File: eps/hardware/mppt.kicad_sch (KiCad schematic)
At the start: 16 parts, among them U43 LTC3130-1

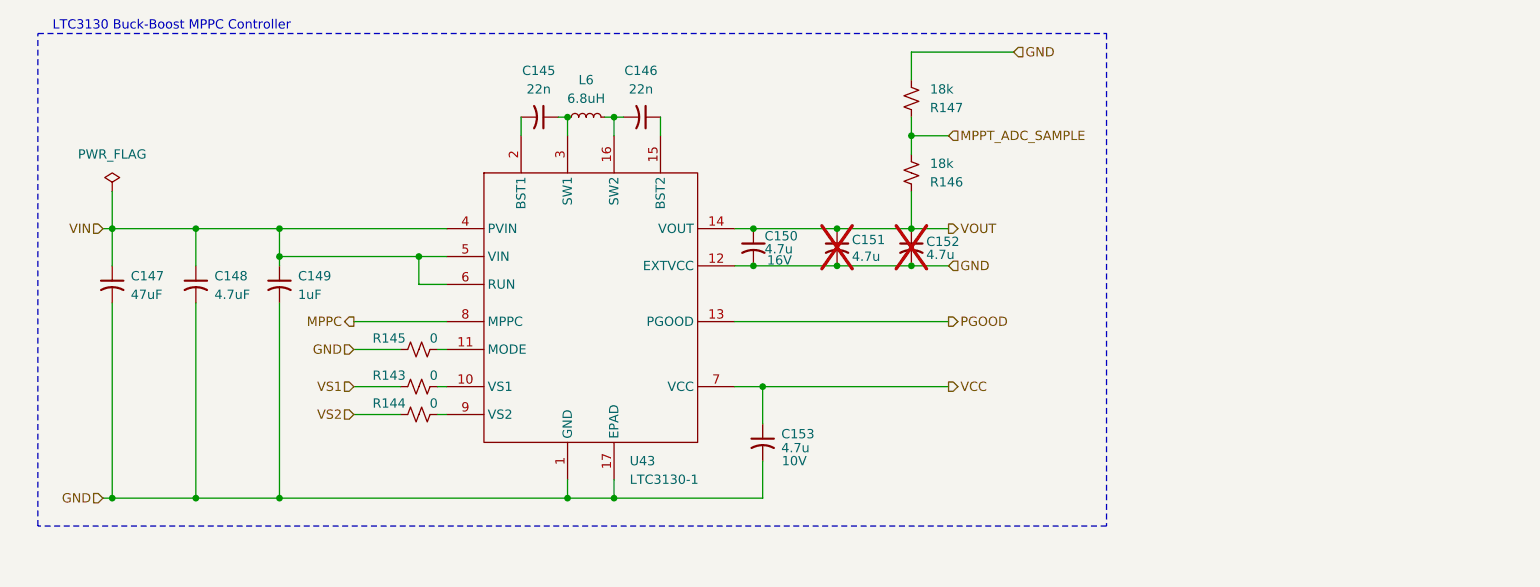
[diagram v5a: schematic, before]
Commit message: fix all ERC errors
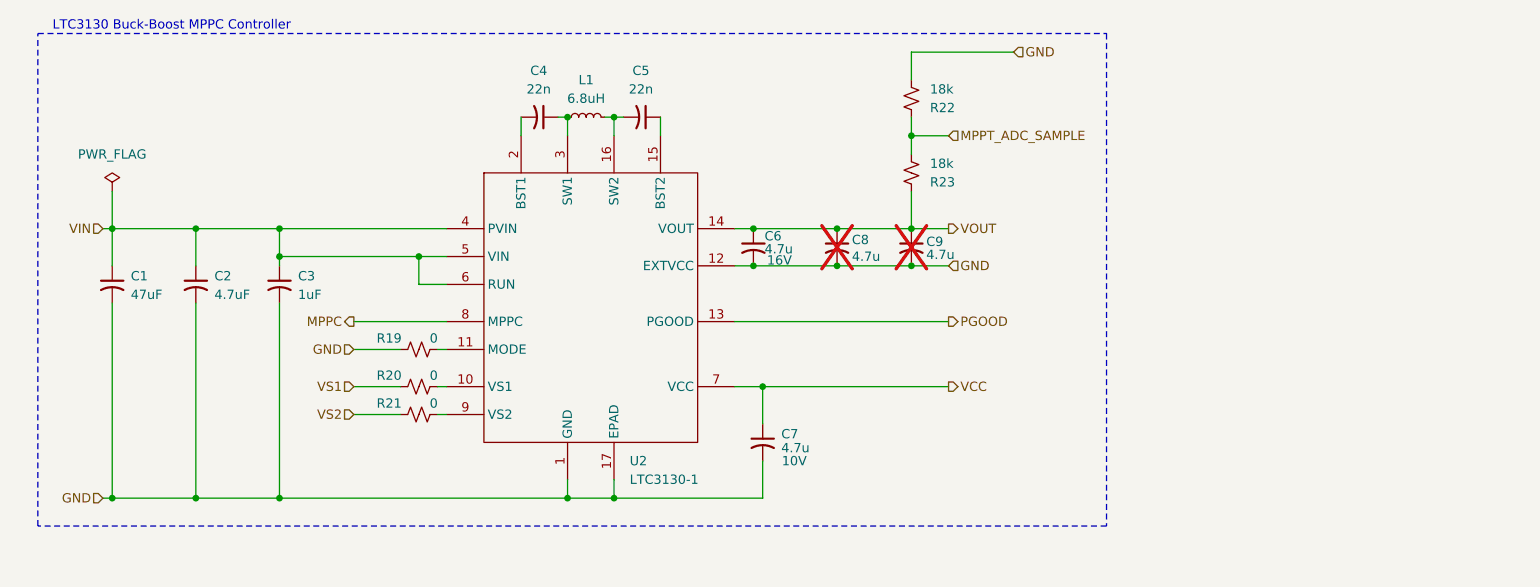
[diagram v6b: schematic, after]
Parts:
- renumbered C147 to C1, C148 to C2, C149 to C3, C145 to C4, C146 to C5, C150 to C6, C153 to C7, C151 to C8, C152 to C9, L6 to L1, R145 to R19, R143 to R20, R144 to R21, R147 to R22, R146 to R23, U43 to U2
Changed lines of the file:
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@@
 		(on_board yes)
 		(dnp no)
-		(property "Reference" "R146"
+		(property "Reference" "R23"
 			(at 135.89 35.5601 0)
 			(effects
@@
 			(project "eps"
 				(path "/9e0ae2e7-d4be-41b4-8312-0d2aceea2180/fa2efaa0-4907-4b3e-94ec-ef462aa79480"
-					(reference "R146")
+					(reference "R23")
 					(unit 1)
 				)
@@
 		(on_board yes)
 		(dnp no)
-		(property "Reference" "C146"
+		(property "Reference" "C5"
 			(at 96.393 20.32 90)
 			(effects
@@
 			(project "eps"
 				(path "/9e0ae2e7-d4be-41b4-8312-0d2aceea2180/fa2efaa0-4907-4b3e-94ec-ef462aa79480"
-					(reference "C146")
+					(reference "C5")
 					(unit 1)
 				)
@@
 		(on_board yes)
 		(dnp no)
-		(property "Reference" "R147"
+		(property "Reference" "R22"
 			(at 135.89 25.4001 0)
 			(effects
@@
 			(project "eps"
 				(path "/9e0ae2e7-d4be-41b4-8312-0d2aceea2180/fa2efaa0-4907-4b3e-94ec-ef462aa79480"
-					(reference "R147")
+					(reference "R22")
 					(unit 1)
 				)
@@
 		(on_board yes)
 		(dnp no)
-		(property "Reference" "C153"
+		(property "Reference" "C7"
 			(at 115.57 69.9769 0)
 			(effects
@@
 			(project ""
 				(path "/9e0ae2e7-d4be-41b4-8312-0d2aceea2180/fa2efaa0-4907-4b3e-94ec-ef462aa79480"
-					(reference "C153")
+					(reference "C7")
 					(unit 1)
 				)
@@
 		(on_board yes)
 		(dnp no)
-		(property "Reference" "C147"
+		(property "Reference" "C1"
 			(at 26.67 48.3869 0)
 			(effects
@@
 			(project "eps"
 				(path "/9e0ae2e7-d4be-41b4-8312-0d2aceea2180/fa2efaa0-4907-4b3e-94ec-ef462aa79480"
-					(reference "C147")
+					(reference "C1")
 					(unit 1)
 				)
@@
 		(on_board yes)
 		(dnp yes)
-		(property "Reference" "C151"
+		(property "Reference" "C8"
 			(at 125.222 43.434 0)
 			(effects
@@
 			(project "eps"
 				(path "/9e0ae2e7-d4be-41b4-8312-0d2aceea2180/fa2efaa0-4907-4b3e-94ec-ef462aa79480"
-					(reference "C151")
+					(reference "C8")
 					(unit 1)
 				)
@@
 		(dnp no)
 		(fields_autoplaced yes)
-		(property "Reference" "L6"
+		(property "Reference" "L1"
 			(at 88.9 21.59 90)
 			(effects
@@
 			(project ""
 				(path "/9e0ae2e7-d4be-41b4-8312-0d2aceea2180/fa2efaa0-4907-4b3e-94ec-ef462aa79480"
-					(reference "L6")
+					(reference "L1")
 					(unit 1)
 				)
@@
 		(on_board yes)
 		(dnp no)
-		(property "Reference" "C149"
+		(property "Reference" "C3"
 			(at 49.53 48.3869 0)
 			(effects
@@
 			(project "eps"
 				(path "/9e0ae2e7-d4be-41b4-8312-0d2aceea2180/fa2efaa0-4907-4b3e-94ec-ef462aa79480"
-					(reference "C149")
+					(reference "C3")
 					(unit 1)
 				)
@@
 		(dnp no)
 		(fields_autoplaced yes)
-		(property "Reference" "U43"
+		(property "Reference" "U2"
 			(at 94.8533 73.66 0)
 			(effects
@@
 			(project ""
 				(path "/9e0ae2e7-d4be-41b4-8312-0d2aceea2180/fa2efaa0-4907-4b3e-94ec-ef462aa79480"
-					(reference "U43")
+					(reference "U2")
 					(unit 1)
 				)
@@
 		(on_board yes)
 		(dnp no)
-		(property "Reference" "C148"
+		(property "Reference" "C2"
 			(at 38.1 48.3869 0)
 			(effects
@@
 			(project "eps"
 				(path "/9e0ae2e7-d4be-41b4-8312-0d2aceea2180/fa2efaa0-4907-4b3e-94ec-ef462aa79480"
-					(reference "C148")
+					(reference "C2")
 					(unit 1)
 				)
@@
 		(on_board yes)
 		(dnp yes)
-		(property "Reference" "C152"
+		(property "Reference" "C9"
 			(at 135.382 43.688 0)
 			(effects
@@
 			(project "eps"
 				(path "/9e0ae2e7-d4be-41b4-8312-0d2aceea2180/fa2efaa0-4907-4b3e-94ec-ef462aa79480"
-					(reference "C152")
+					(reference "C9")
 					(unit 1)
 				)
@@
 		(on_board yes)
 		(dnp no)
-		(property "Reference" "R143"
+		(property "Reference" "R20"
 			(at 61.976 61.976 90)
 			(effects
@@
 			(project ""
 				(path "/9e0ae2e7-d4be-41b4-8312-0d2aceea2180/fa2efaa0-4907-4b3e-94ec-ef462aa79480"
-					(reference "R143")
+					(reference "R20")
 					(unit 1)
 				)
@@
 		(on_board yes)
 		(dnp no)
-		(property "Reference" "R144"
+		(property "Reference" "R21"
 			(at 61.976 65.786 90)
 			(effects
@@
 			(project "eps"
 				(path "/9e0ae2e7-d4be-41b4-8312-0d2aceea2180/fa2efaa0-4907-4b3e-94ec-ef462aa79480"
-					(reference "R144")
+					(reference "R21")
 					(unit 1)
 				)
@@
 		(on_board yes)
 		(dnp no)
-		(property "Reference" "C150"
+		(property "Reference" "C6"
 			(at 113.284 42.926 0)
 			(effects
@@
 			(project ""
 				(path "/9e0ae2e7-d4be-41b4-8312-0d2aceea2180/fa2efaa0-4907-4b3e-94ec-ef462aa79480"
-					(reference "C150")
+					(reference "C6")
 					(unit 1)
 				)
@@
 		(on_board yes)
 		(dnp no)
-		(property "Reference" "R145"
+		(property "Reference" "R19"
 			(at 61.976 56.896 90)
 			(effects
@@
 			(project "eps"
 				(path "/9e0ae2e7-d4be-41b4-8312-0d2aceea2180/fa2efaa0-4907-4b3e-94ec-ef462aa79480"
-					(reference "R145")
+					(reference "R19")
 					(unit 1)
 				)
@@
 		(on_board yes)
 		(dnp no)
-		(property "Reference" "C145"
+		(property "Reference" "C4"
 			(at 82.423 20.32 90)
 			(effects
@@
 			(project ""
 				(path "/9e0ae2e7-d4be-41b4-8312-0d2aceea2180/fa2efaa0-4907-4b3e-94ec-ef462aa79480"
-					(reference "C145")
+					(reference "C4")
 					(unit 1)
 				)
@@
 		(dnp no)
 		(fields_autoplaced yes)
-		(property "Reference" "#FLG04"
+		(property "Reference" "#FLG02"
 			(at 24.13 34.925 0)
 			(effects
@@
 			(project "eps"
 				(path "/9e0ae2e7-d4be-41b4-8312-0d2aceea2180/fa2efaa0-4907-4b3e-94ec-ef462aa79480"
-					(reference "#FLG04")
-					(unit 1)
-				)
+					(reference "#FLG02")
+					(unit 1)
+				)

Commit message: netlist fixes
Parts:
- renumbered R22 to R10, R23 to R11, R19 to R7, R20 to R8, R21 to R9
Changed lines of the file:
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@@
 		(on_board yes)
 		(dnp no)
-		(property "Reference" "R23"
+		(property "Reference" "R11"
 			(at 135.89 35.5601 0)
 			(effects
@@
 			(project "eps"
 				(path "/9e0ae2e7-d4be-41b4-8312-0d2aceea2180/fa2efaa0-4907-4b3e-94ec-ef462aa79480"
-					(reference "R23")
+					(reference "R11")
 					(unit 1)
 				)
@@
 		(on_board yes)
 		(dnp no)
-		(property "Reference" "R22"
+		(property "Reference" "R10"
 			(at 135.89 25.4001 0)
 			(effects
@@
 			(project "eps"
 				(path "/9e0ae2e7-d4be-41b4-8312-0d2aceea2180/fa2efaa0-4907-4b3e-94ec-ef462aa79480"
-					(reference "R22")
+					(reference "R10")
 					(unit 1)
 				)
@@
 		(on_board yes)
 		(dnp no)
-		(property "Reference" "R20"
+		(property "Reference" "R8"
 			(at 61.976 61.976 90)
 			(effects
@@
 			(project ""
 				(path "/9e0ae2e7-d4be-41b4-8312-0d2aceea2180/fa2efaa0-4907-4b3e-94ec-ef462aa79480"
-					(reference "R20")
+					(reference "R8")
 					(unit 1)
 				)
@@
 		(on_board yes)
 		(dnp no)
-		(property "Reference" "R21"
+		(property "Reference" "R9"
 			(at 61.976 65.786 90)
 			(effects
@@
 			(project "eps"
 				(path "/9e0ae2e7-d4be-41b4-8312-0d2aceea2180/fa2efaa0-4907-4b3e-94ec-ef462aa79480"
-					(reference "R21")
+					(reference "R9")
 					(unit 1)
 				)
@@
 		(on_board yes)
 		(dnp no)
-		(property "Reference" "R19"
+		(property "Reference" "R7"
 			(at 61.976 56.896 90)
 			(effects
@@
 			(project "eps"
 				(path "/9e0ae2e7-d4be-41b4-8312-0d2aceea2180/fa2efaa0-4907-4b3e-94ec-ef462aa79480"
-					(reference "R19")
+					(reference "R7")
 					(unit 1)
 				)
@@
 		(dnp no)
 		(fields_autoplaced yes)
-		(property "Reference" "#FLG02"
+		(property "Reference" "#FLG03"
 			(at 24.13 34.925 0)
 			(effects
@@
 			(project "eps"
 				(path "/9e0ae2e7-d4be-41b4-8312-0d2aceea2180/fa2efaa0-4907-4b3e-94ec-ef462aa79480"
-					(reference "#FLG02")
-					(unit 1)
-				)
+					(reference "#FLG03")
+					(unit 1)
+				)

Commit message: start footprint assignment
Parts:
- C1, C2, C3, C4, C5, C6, C7, C8, C9: footprint (none) -> Capacitor_SMD:C_0603_1608Metric
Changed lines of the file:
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@@
 			)
 		)
-		(property "Footprint" ""
+		(property "Footprint" "Capacitor_SMD:C_0603_1608Metric"
 			(at 96.52 26.67 0)
 			(effects
@@
 			)
 		)
-		(property "Footprint" ""
+		(property "Footprint" "Capacitor_SMD:C_0603_1608Metric"
 			(at 113.03 71.12 0)
 			(effects
@@
 			)
 		)
-		(property "Footprint" ""
+		(property "Footprint" "Capacitor_SMD:C_0603_1608Metric"
 			(at 24.13 49.53 0)
 			(effects
@@
 			)
 		)
-		(property "Footprint" ""
+		(property "Footprint" "Capacitor_SMD:C_0603_1608Metric"
 			(at 123.19 44.45 0)
 			(effects
@@
 			)
 		)
-		(property "Footprint" ""
+		(property "Footprint" "Capacitor_SMD:C_0603_1608Metric"
 			(at 46.99 49.53 0)
 			(effects
@@
 			)
 		)
-		(property "Footprint" ""
+		(property "Footprint" "Capacitor_SMD:C_0603_1608Metric"
 			(at 35.56 49.53 0)
 			(effects
@@
 			)
 		)
-		(property "Footprint" ""
+		(property "Footprint" "Capacitor_SMD:C_0603_1608Metric"
 			(at 133.35 44.45 0)
 			(effects
@@
 			)
 		)
-		(property "Footprint" ""
+		(property "Footprint" "Capacitor_SMD:C_0603_1608Metric"
 			(at 111.76 44.45 0)
 			(effects
@@
 			)
 		)
-		(property "Footprint" ""
+		(property "Footprint" "Capacitor_SMD:C_0603_1608Metric"
 			(at 82.55 26.67 0)
 			(effects
